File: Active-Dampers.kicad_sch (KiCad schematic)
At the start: 32 parts, among them J2 Conn_01x04, J3 Conn_01x04, J4 Conn_01x02, J5 Conn_01x04, J6 USB_C_Receptacle_USB2.0_16P, J7 Conn_01x04, J8 Barrel_Jack_Switch_Pin3Ring, SW2 SW_SPST, U10 L80-R, U2 DRV8848, U3 ESP32-S3-MINI-1, U4 DRV8848, U5 DRV8848, U7 DRV8848

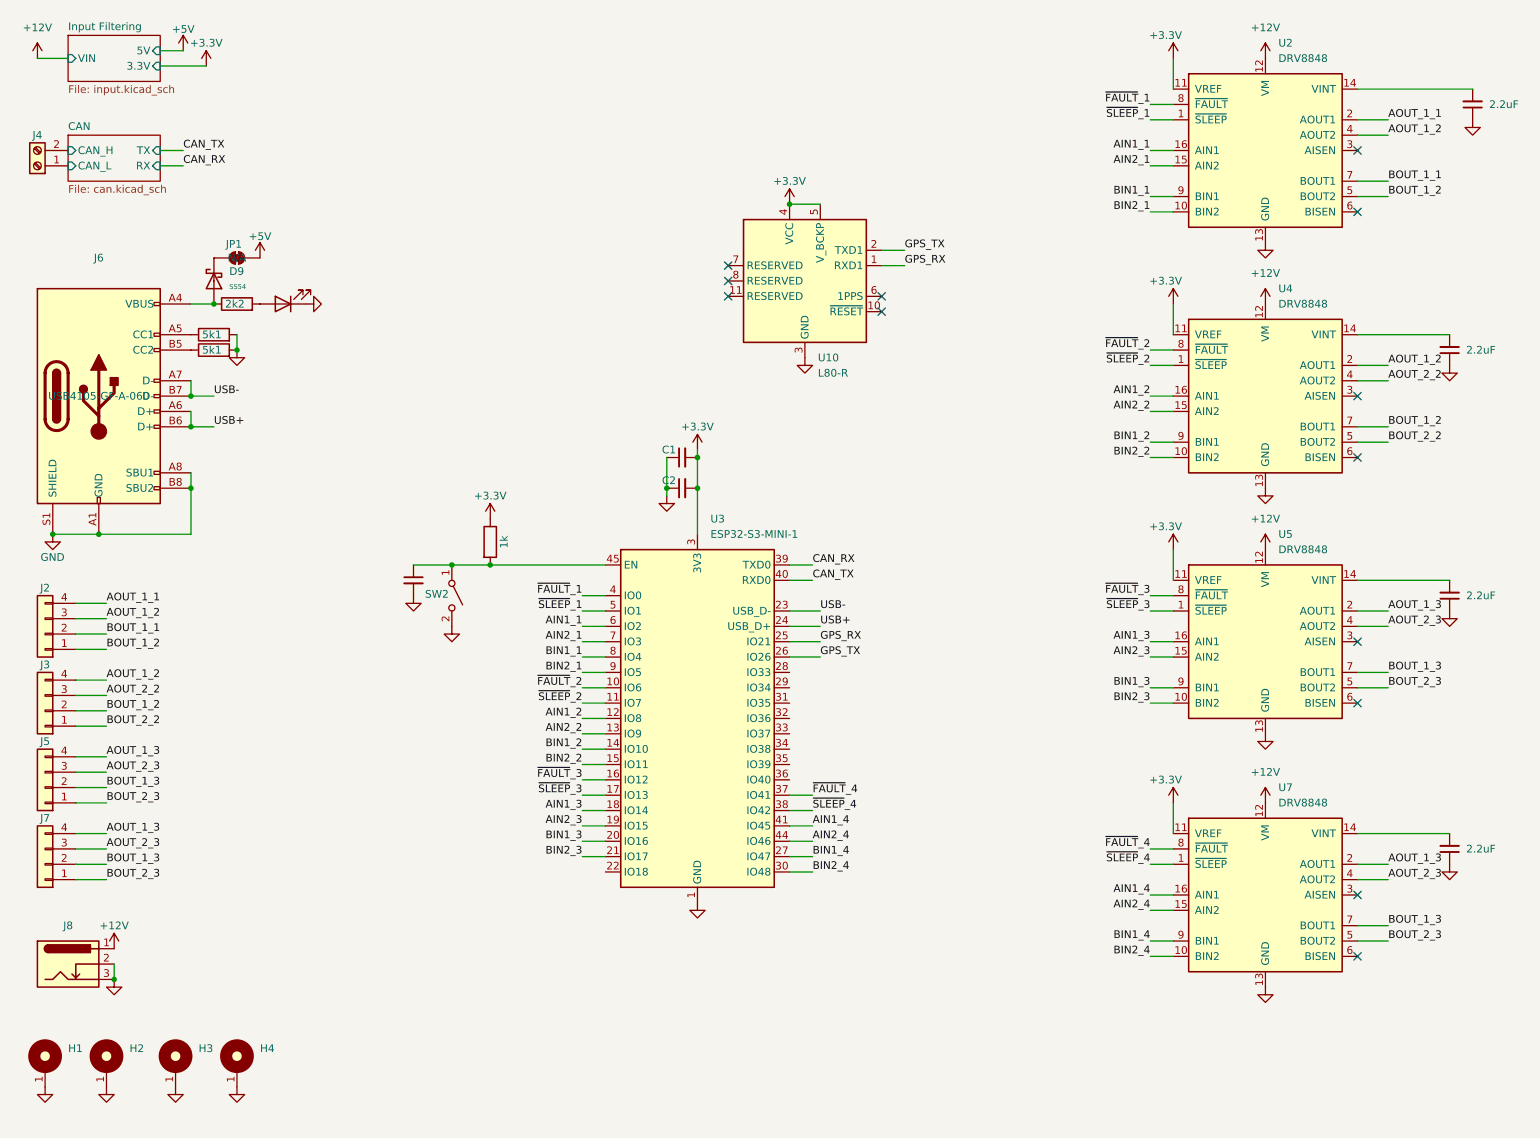
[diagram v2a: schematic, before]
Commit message: add cubemx project and redo some layour with new parts
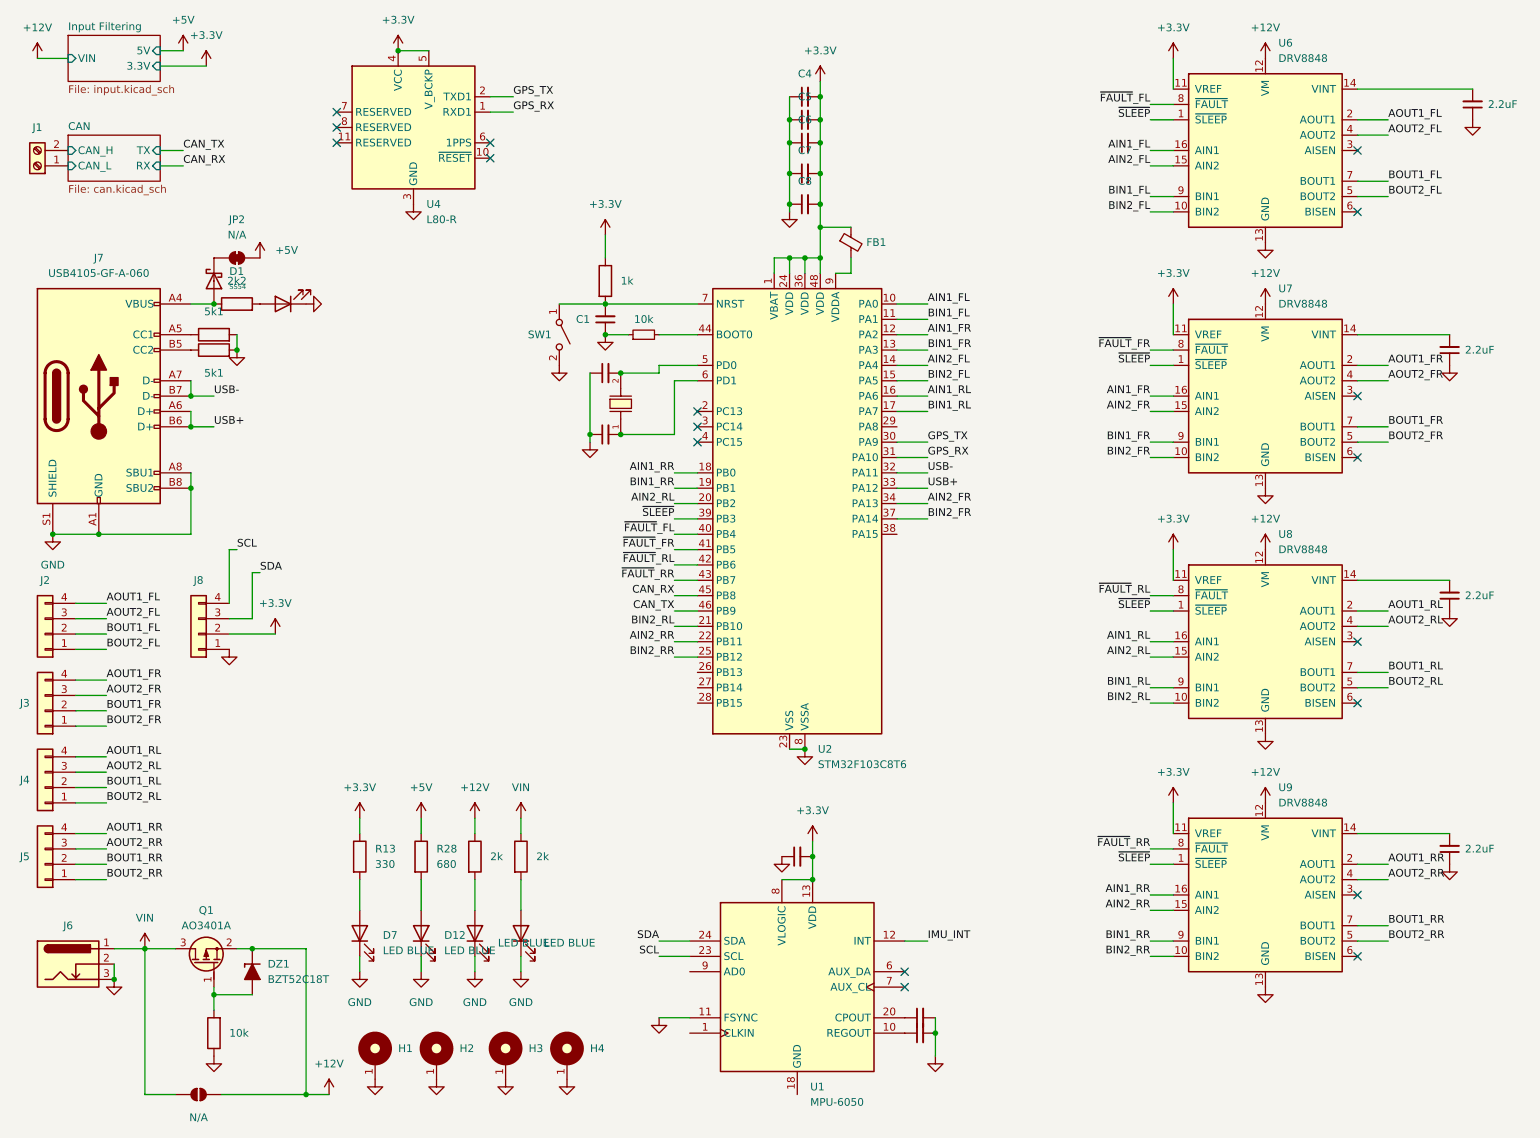
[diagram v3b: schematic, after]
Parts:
- removed C22: 10uF, PCM_Capacitor_SMD_AKL:C_0603_1608Metric, symbol Device:C_Small
- removed U3: ESP32-S3-MINI-1, RF_Module:ESP32-S2-MINI-1, symbol RF_Module:ESP32-S3-MINI-1
- added C10: 2.2nF, PCM_Capacitor_SMD_AKL:C_0603_1608Metric, symbol Device:C_Small
- added C3: 22pF, PCM_Capacitor_SMD_AKL:C_0603_1608Metric, symbol Device:C_Small
- added C34: 0.1uF, PCM_Capacitor_SMD_AKL:C_0603_1608Metric, symbol Device:C_Small
- added C4, C5, C8, C9: 10uF, PCM_Capacitor_SMD_AKL:C_0603_1608Metric, symbol Device:C_Small
- added C6: 100nF, PCM_Capacitor_SMD_AKL:C_0603_1608Metric, symbol Device:C_Small
- added C7: 1uF, PCM_Capacitor_SMD_AKL:C_0603_1608Metric, symbol Device:C_Small
- added D12, D14, D19, D7: LED BLUE, LED_SMD:LED_0603_1608Metric, symbol Device:LED
- added DZ1: BZT52C18T, PCM_Diode_SMD_AKL:D_SOD-523, symbol PCM_Diode_Zener_AKL:BZT52C18T
- added FB1: MMZ1005F181ETD25, PCM_Ferrite_SMD_AKL:Ferrite_0402_1005Metric, symbol Device:FerriteBead_Small
- added J8: OLED, PCM_SparkFun-Display:OLED_0.96, symbol Connector_Generic:Conn_01x04
- added JP1: SolderJumper_2_Open, Jumper:SolderJumper-2_P1.3mm_Open_Pad1.0x1.5mm, symbol Jumper:SolderJumper_2_Open
- added Q1: AO3401A, PCM_Package_TO_SOT_SMD_AKL:SOT-23, symbol PCM_Transistor_MOSFET_AKL:AO3401A
- added R13: 330, PCM_Resistor_SMD_AKL:R_0603_1608Metric, symbol Device:R
- added R2: 10k, PCM_Resistor_SMD_AKL:R_0603_1608Metric, symbol Device:R_Small
- added R28: 680, PCM_Resistor_SMD_AKL:R_0603_1608Metric, symbol Device:R
- added R30, R36: 2k, PCM_Resistor_SMD_AKL:R_0603_1608Metric, symbol Device:R
- added R5: 10k, PCM_Resistor_SMD_AKL:R_0603_1608Metric, symbol Device:R
- added U1: MPU-6050, PCM_SparkFun-Semiconductor-Standard:QFN-24-1EP_4x4mm_P0.5mm, symbol PCM_SparkFun-Sensor:MPU-6050
- added U2: STM32F103C8T6, PCM_JLCPCB:LQFP-48_7x7mm_P0.5mm, symbol PCM_JLCPCB-MCUs:STM32F103C8T6
- added X1: X50328MSB2GI, PCM_JLCPCB:CRYSTAL-SMD_L5.0-W3.2, symbol PCM_JLCPCB-Crystals:Crystal, 8MHz, 20pF, ±10ppm
- C1: value 1uF -> 100nF; Manufacturer_Part_Number TMK105BJ105MV-F -> MCASU105SB5104MFNA01
- C2: value 10uF -> 22pF; Manufacturer_Part_Number CL05A106MP5NUNC -> MCASU105SB5104MFNA01
- J2: value Conn_01x04 -> FL
- J3: value Conn_01x04 -> FR
- J4: renamed from J5; value Conn_01x04 -> RL
- J5: renamed from J7; value Conn_01x04 -> RR
- renumbered C21 to C11, C23 to C12, C24 to C13, C20 to C14, D9 to D1, D8 to D2, J4 to J1, J8 to J6, J6 to J7, JP1 to JP2, R23 to R1, R6 to R3, R7 to R4, R8 to R6, SW2 to SW1, U10 to U4, U2 to U6, U4 to U7, U5 to U8, U7 to U9
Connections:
- net ~{SLEEP}_2 is gone; now on net ~{SLEEP}: U7.1 (~{SLEEP})
- net ~{SLEEP}_3 is gone; now on net ~{SLEEP}: U8.1 (~{SLEEP})
- net ~{SLEEP}_4 is gone; now on net ~{SLEEP}: U9.1 (~{SLEEP})
- net +12V: now also DZ1.1 (K), JP1.2 (B), Q1.2 (S), R30.1; no longer J6.1
- net +3.3V: now also C4.2, C5.2, C6.2, C7.2, C8.2, C9.2, FB1.1, J8.2 (Pin_2), R13.1, U1.13 (VDD), U1.8 (VLOGIC), U2.1 (VBAT), U2.24 (VDD), U2.36 (VDD), U2.48 (VDD); no longer C1.2, C2.2
- net +5V: now also R28.1
- net CAN_RX: now also U2.45 (PB8)
- net CAN_TX: now also U2.46 (PB9)
- net GND: now also C10.2, C3.1, C34.2, C4.1, C5.1, C6.1, C7.1, C8.1, C9.1, D12.1 (K), D14.1 (K), D19.1 (K), D7.1 (K), J8.1 (Pin_1), R2.1, R5.1, U1.11 (FSYNC), U2.23 (VSS), U2.35 (VSS), U2.47 (VSS), U2.8 (VSSA)
- net GPS_RX: now also U2.31 (PA10)
- net GPS_TX: now also U2.30 (PA9)
- net USB+: now also U2.33 (PA12)
- net USB-: now also U2.32 (PA11)
- net at R1.2, SW1.1 (A): now also C1.2, U2.7 (NRST)
- net AIN1_1 renamed AIN1_FL
- net AIN1_FL: now also U2.10 (PA0)
- net AIN1_2 renamed AIN1_FR
- net AIN1_FR: now also U2.12 (PA2)
- net AIN1_3 renamed AIN1_RL
- net AIN1_RL: now also U2.16 (PA6)
- net AIN1_4 renamed AIN1_RR
- net AIN1_RR: now also U2.18 (PB0)
- net AIN2_1 renamed AIN2_FL
- net AIN2_FL: now also U2.14 (PA4)
- net AIN2_2 renamed AIN2_FR
- net AIN2_FR: now also U2.34 (PA13)
- net AIN2_3 renamed AIN2_RL
- net AIN2_RL: now also U2.20 (PB2)
- net AIN2_4 renamed AIN2_RR
- net AIN2_RR: now also U2.22 (PB11)
- net AOUT_1_1 renamed AOUT1_FL
- net AOUT_1_2 renamed AOUT1_FR
- net AOUT1_FR: no longer J2.3 (Pin_3), U6.4 (AOUT2)
- net AOUT_1_3 renamed AOUT1_RL
- net AOUT1_RL: no longer J5.4 (Pin_4), U9.2 (AOUT1)
- net AOUT_2_2 renamed AOUT2_FR
- net AOUT_2_3 renamed AOUT2_RL
- net AOUT2_RL: no longer J5.3 (Pin_3), U9.4 (AOUT2)
- net BIN1_1 renamed BIN1_FL
- net BIN1_FL: now also U2.11 (PA1)
- net BIN1_2 renamed BIN1_FR
- net BIN1_FR: now also U2.13 (PA3)
- net BIN1_3 renamed BIN1_RL
- net BIN1_RL: now also U2.17 (PA7)
- net BIN1_4 renamed BIN1_RR
- net BIN1_RR: now also U2.19 (PB1)
- net BIN2_1 renamed BIN2_FL
- net BIN2_FL: now also U2.15 (PA5)
- net BIN2_2 renamed BIN2_FR
- net BIN2_FR: now also U2.37 (PA14)
- net BIN2_3 renamed BIN2_RL
- net BIN2_RL: now also U2.21 (PB10)
- net BIN2_4 renamed BIN2_RR
- net BIN2_RR: now also U2.25 (PB12)
- net BOUT_1_1 renamed BOUT1_FL
- net BOUT_1_2 renamed BOUT1_FR
- net BOUT1_FR: no longer J2.1 (Pin_1), U6.5 (BOUT2)
- net BOUT_1_3 renamed BOUT1_RL
- net BOUT1_RL: no longer J5.2 (Pin_2), U9.7 (BOUT1)
- net BOUT_2_2 renamed BOUT2_FR
- net BOUT_2_3 renamed BOUT2_RL
- net BOUT2_RL: no longer J5.1 (Pin_1), U9.5 (BOUT2)
- net ~{FAULT}_1 renamed ~{FAULT}_FL
- net ~{FAULT}_FL: now also U2.40 (PB4)
- net ~{FAULT}_2 renamed ~{FAULT}_FR
- net ~{FAULT}_FR: now also U2.41 (PB5)
- net ~{FAULT}_3 renamed ~{FAULT}_RL
- net ~{FAULT}_RL: now also U2.42 (PB6)
- net ~{FAULT}_4 renamed ~{FAULT}_RR
- net ~{FAULT}_RR: now also U2.43 (PB7)
- net ~{SLEEP}_1 renamed ~{SLEEP}
- net ~{SLEEP}: now also U2.39 (PB3)
- new net: D7.2 (A), R13.2
- new net: FB1.2, U2.9 (VDDA)
- new net: R2.2, U2.44 (BOOT0)
- new net: C2.2, U2.5 (PD0), X1.2
- new net: C3.2, U2.6 (PD1), X1.1
- new net: DZ1.2 (A), Q1.1 (G), R5.2
- new net: D14.2 (A), R30.2
- new net: D19.2 (A), R36.2
- new net: D12.2 (A), R28.2
- new net: C34.1, U1.10 (REGOUT)
- new net: C10.1, U1.20 (CPOUT)
- new net AOUT1_RR: J5.4 (Pin_4), U9.2 (AOUT1)
- new net AOUT2_FL: J2.3 (Pin_3), U6.4 (AOUT2)
- new net AOUT2_RR: J5.3 (Pin_3), U9.4 (AOUT2)
- new net BOUT1_RR: J5.2 (Pin_2), U9.7 (BOUT1)
- new net BOUT2_FL: J2.1 (Pin_1), U6.5 (BOUT2)
- new net BOUT2_RR: J5.1 (Pin_1), U9.5 (BOUT2)
- new net IMU_INT: U1.12 (INT)
- new net SCL: J8.4 (Pin_4), U1.23 (SCL)
- new net SDA: J8.3 (Pin_3), U1.24 (SDA)
- new net VIN: J6.1, JP1.1 (A), Q1.3 (D), R36.1
- no-connect marks 13 -> 18
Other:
- moved on the sheet: H1, H2, H3, H4, SW1, U4
